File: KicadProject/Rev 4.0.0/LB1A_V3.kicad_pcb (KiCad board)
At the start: 6 copper layers, 42 x 42 mm, 187 parts, among them J601 2337019-1, J602 2337019-1, U101 STM32MP157CAA3, U201 AS4C256M16D3LC-12BCN, U401 STPMIC1xPQR, U501 S40FC004C1B2C00000, U601 LBEE59B1LV-278, U701 DF40C-70DP-0.4V(51), U702 DF40C-100DP-0.4V(51), U703 DF40C-100DP-0.4V(51), X101 32.768kHz, Y101 24MHz

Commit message: power planes
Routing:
- net PMIC_LDO5_2V9: track 0.75 -> 10.7 mm, vias 1 -> 3
- net PMIC_VOUT4_3V3: vias 3 -> 7
- added copper zone on B.Cu, net PMIC_VOUT4_3V3
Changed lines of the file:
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@@
     (thickness 1.2)
     (drawings 8)
-    (tracks 720)
+    (tracks 734)
     (zones 0)
     (modules 187)
@@
   )
   (setup
-    (last_trace_width 0.254)
+    (last_trace_width 0.4)
     (user_trace_width 0.1)
     (user_trace_width 0.127)
@@
   (segment (start 180.5 103.5) (end 180 103.5) (width 0.2) (layer L1_Sig_Pwr.Cu) (net 13))
   (via (at 180.5 103.5) (size 0.4) (drill 0.2) (layers L1_Sig_Pwr.Cu L6_Sig_Pwr.Cu) (net 13))
+  (via (at 172.4 104.1) (size 0.4) (drill 0.2) (layers L1_Sig_Pwr.Cu L6_Sig_Pwr.Cu) (net 13))
+  (via (at 173.6 104.1) (size 0.4) (drill 0.2) (layers L1_Sig_Pwr.Cu L6_Sig_Pwr.Cu) (net 13))
+  (via (at 172.4 104.7) (size 0.4) (drill 0.2) (layers L1_Sig_Pwr.Cu L6_Sig_Pwr.Cu) (net 13))
+  (via (at 173.6 104.7) (size 0.4) (drill 0.2) (layers L1_Sig_Pwr.Cu L6_Sig_Pwr.Cu) (net 13))
   (via (at 179.4 99.6) (size 0.4) (drill 0.2) (layers L1_Sig_Pwr.Cu L6_Sig_Pwr.Cu) (net 18))
   (via (at 172.5 95.6) (size 0.4) (drill 0.2) (layers L1_Sig_Pwr.Cu L6_Sig_Pwr.Cu) (net 18))
@@
   (segment (start 178.746829 98.2) (end 178.675937 98.270892) (width 0.254) (layer L1_Sig_Pwr.Cu) (net 24))
   (segment (start 179.4 98.2) (end 178.746829 98.2) (width 0.254) (layer L1_Sig_Pwr.Cu) (net 24))
+  (segment (start 180.595892 98.270892) (end 180.725 98.4) (width 0.4) (layer L6_Sig_Pwr.Cu) (net 24))
+  (segment (start 178.675937 98.270892) (end 180.595892 98.270892) (width 0.4) (layer L6_Sig_Pwr.Cu) (net 24))
+  (segment (start 180.725 98.4) (end 181.057522 98.4) (width 0.4) (layer L6_Sig_Pwr.Cu) (net 24))
+  (segment (start 181.057522 98.4) (end 181.52499 98.867468) (width 0.4) (layer L6_Sig_Pwr.Cu) (net 24))
+  (segment (start 181.599999 98.942477) (end 181.599999 104.399999) (width 0.4) (layer L6_Sig_Pwr.Cu) (net 24))
+  (segment (start 181.52499 98.867468) (end 181.599999 98.942477) (width 0.4) (layer L6_Sig_Pwr.Cu) (net 24))
+  (via (at 182.1 104.9) (size 0.4) (drill 0.2) (layers L1_Sig_Pwr.Cu L6_Sig_Pwr.Cu) (net 24))
+  (segment (start 181.599999 104.399999) (end 182.1 104.9) (width 0.4) (layer L6_Sig_Pwr.Cu) (net 24))
+  (via (at 182.7 104.9) (size 0.4) (drill 0.2) (layers L1_Sig_Pwr.Cu L6_Sig_Pwr.Cu) (net 24))
+  (segment (start 182.1 104.9) (end 182.7 104.9) (width 0.4) (layer L6_Sig_Pwr.Cu) (net 24))
   (segment (start 183.35 94.75) (end 183.35 93.95) (width 0.127) (layer L1_Sig_Pwr.Cu) (net 35))
   (segment (start 183.35 93.95) (end 183.60402 93.69598) (width 0.127) (layer L1_Sig_Pwr.Cu) (net 35))
@@
         (xy 198.9 116.8) (xy 199.7 116.8) (xy 199.7 116) (xy 200.5 116) (xy 200.5 115.2)
         (xy 201.3 115.2) (xy 201.3 114.4) (xy 201.6 114.4) (xy 201.6 112.5) (xy 213 112.5)
-        (xy 213 130) (xy 185.6 130) (xy 185.6 104.4) (xy 182.8 104.4) (xy 182.8 101)
+        (xy 213 130) (xy 186.5 130) (xy 186.5 104.4) (xy 182.8 104.4) (xy 182.8 101)
         (xy 187.4 101) (xy 187.4 98.1) (xy 182.4 98.1) (xy 182.4 93.1) (xy 189.2 93.1)
       )
@@
       )
     )
+  )
+  (zone (net 13) (net_name PMIC_VOUT4_3V3) (layer L6_Sig_Pwr.Cu) (hatch none 0.508)
+    (connect_pads yes (clearance 0.1))
+    (min_thickness 0.1)
+    (fill yes (arc_segments 32) (thermal_gap 0.508) (thermal_bridge_width 0.508))
+    (polygon
+      (pts
+        (xy 174.8 105) (xy 171 105) (xy 171 102.6) (xy 174.8 102.6)
+      )
+    )

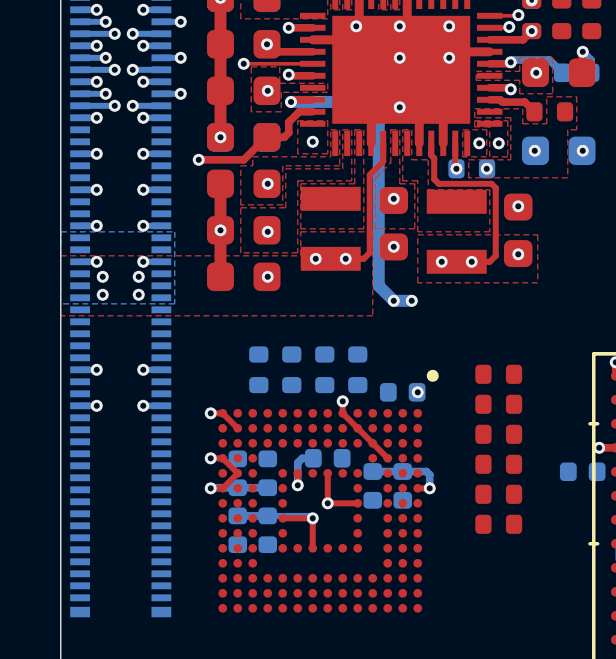
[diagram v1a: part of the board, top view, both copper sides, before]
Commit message: L3 polygon complete
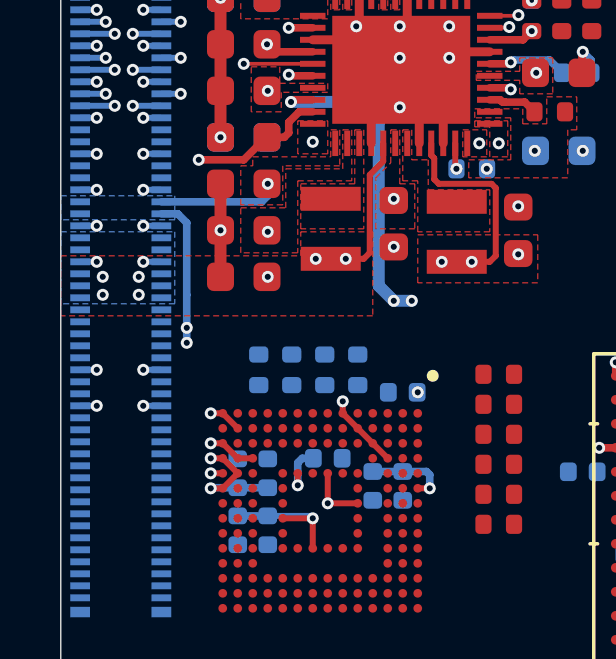
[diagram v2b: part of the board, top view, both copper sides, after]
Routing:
- net PMIC_LDO1_1V8: track 0.00 -> 9.00 mm, vias 1 -> 3
- net PMIC_LDO5_2V9: track 10.7 -> 12.7 mm, vias 3 -> 5
- added copper zone on B.Cu, net PMIC_LDO1_1V8
- added copper zone on L3_Sig_Pwr.Cu, net PMIC_LDO1_1V8
- added copper zone on L3_Sig_Pwr.Cu, net PMIC_LDO5_2V9
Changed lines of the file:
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@@
     (thickness 1.2)
     (drawings 8)
-    (tracks 734)
+    (tracks 751)
     (zones 0)
     (modules 187)
@@
   )
   (setup
-    (last_trace_width 0.4)
+    (last_trace_width 0.254)
     (user_trace_width 0.1)
     (user_trace_width 0.127)
@@
   (segment (start 187.292999 96.872999) (end 186.077001 96.872999) (width 0.254) (layer L6_Sig_Pwr.Cu) (net 20))
   (segment (start 187.72 97.3) (end 187.292999 96.872999) (width 0.254) (layer L6_Sig_Pwr.Cu) (net 20))
+  (segment (start 177.9 101.4) (end 177.9 101) (width 0.254) (layer L6_Sig_Pwr.Cu) (net 21))
+  (segment (start 177.7 101.6) (end 177.9 101.4) (width 0.254) (layer L6_Sig_Pwr.Cu) (net 21))
+  (segment (start 174.355 101.6) (end 177.7 101.6) (width 0.254) (layer L6_Sig_Pwr.Cu) (net 21))
+  (segment (start 174.355 102) (end 174.9 102) (width 0.254) (layer L6_Sig_Pwr.Cu) (net 21))
+  (segment (start 174.9 102) (end 175.2 102.3) (width 0.254) (layer L6_Sig_Pwr.Cu) (net 21))
+  (segment (start 175.2 102.3) (end 175.2 104.7) (width 0.254) (layer L6_Sig_Pwr.Cu) (net 21))
+  (via (at 175.2 105.8) (size 0.4) (drill 0.2) (layers L1_Sig_Pwr.Cu L6_Sig_Pwr.Cu) (net 21))
+  (segment (start 175.2 104.7) (end 175.2 105.8) (width 0.254) (layer L6_Sig_Pwr.Cu) (net 21))
+  (via (at 175.2 106.3) (size 0.4) (drill 0.2) (layers L1_Sig_Pwr.Cu L6_Sig_Pwr.Cu) (net 21))
+  (segment (start 175.2 105.8) (end 175.2 106.3) (width 0.254) (layer L6_Sig_Pwr.Cu) (net 21))
   (segment (start 177.875 99.45) (end 177.85 99.45) (width 0.254) (layer L1_Sig_Pwr.Cu) (net 22))
   (via (at 175.6 100.2) (size 0.4) (drill 0.2) (layers L1_Sig_Pwr.Cu L6_Sig_Pwr.Cu) (net 22))
@@
   (via (at 182.7 104.9) (size 0.4) (drill 0.2) (layers L1_Sig_Pwr.Cu L6_Sig_Pwr.Cu) (net 24))
   (segment (start 182.1 104.9) (end 182.7 104.9) (width 0.4) (layer L6_Sig_Pwr.Cu) (net 24))
+  (segment (start 177.4 110.15) (end 176.9 110.15) (width 0.2) (layer L1_Sig_Pwr.Cu) (net 24))
+  (segment (start 176.9 110.15) (end 176.4 109.65) (width 0.2) (layer L1_Sig_Pwr.Cu) (net 24))
+  (via (at 176 109.649997) (size 0.4) (drill 0.2) (layers L1_Sig_Pwr.Cu L6_Sig_Pwr.Cu) (net 24))
+  (segment (start 176.000003 109.65) (end 176 109.649997) (width 0.2) (layer L1_Sig_Pwr.Cu) (net 24))
+  (segment (start 176.4 109.65) (end 176.000003 109.65) (width 0.2) (layer L1_Sig_Pwr.Cu) (net 24))
+  (via (at 176 110.65) (size 0.4) (drill 0.2) (layers L1_Sig_Pwr.Cu L6_Sig_Pwr.Cu) (net 24))
+  (segment (start 176.4 110.65) (end 176 110.65) (width 0.2) (layer L1_Sig_Pwr.Cu) (net 24))
   (segment (start 183.35 94.75) (end 183.35 93.95) (width 0.127) (layer L1_Sig_Pwr.Cu) (net 35))
   (segment (start 183.35 93.95) (end 183.60402 93.69598) (width 0.127) (layer L1_Sig_Pwr.Cu) (net 35))
@@
       (pts
         (xy 182.3 98.2) (xy 187.3 98.2) (xy 187.3 99) (xy 187.3 100.9) (xy 182.7 100.9)
-        (xy 182.7 102.2) (xy 178.9 102.2) (xy 178.9 103.4) (xy 171 103.4) (xy 171 88)
-        (xy 178.3 88) (xy 178.3 90.3) (xy 182.3 90.3)
+        (xy 182.7 104.4) (xy 178.9 104.4) (xy 171 104.4) (xy 171 88) (xy 178.3 88)
+        (xy 178.3 90.3) (xy 182.3 90.3)
       )
     )
@@
       )
     )
+  )
+  (zone (net 24) (net_name PMIC_LDO5_2V9) (layer L3_Sig_Pwr.Cu) (hatch none 0.508)
+    (connect_pads yes (clearance 0.1))
+    (min_thickness 0.1)
+    (fill yes (arc_segments 32) (thermal_gap 0.508) (thermal_bridge_width 0.508))
+    (polygon
+      (pts
+        (xy 186.4 113.4) (xy 175.7 113.4) (xy 175.7 104.5) (xy 186.4 104.5)
+      )
+    )
+  )
+  (zone (net 21) (net_name PMIC_LDO1_1V8) (layer L6_Sig_Pwr.Cu) (hatch none 0.508)
+    (connect_pads yes (clearance 0.1))
+    (min_thickness 0.1)
+    (fill yes (arc_segments 32) (thermal_gap 0.508) (thermal_bridge_width 0.508))
+    (polygon
+      (pts
+        (xy 174.8 102.2) (xy 171 102.2) (xy 171 101.4) (xy 174.8 101.4)
+      )
+    )
+  )
+  (zone (net 21) (net_name PMIC_LDO1_1V8) (layer L3_Sig_Pwr.Cu) (hatch none 0.508)
+    (connect_pads yes (clearance 0.1))
+    (min_thickness 0.1)
+    (fill yes (arc_segments 32) (thermal_gap 0.508) (thermal_bridge_width 0.508))
+    (polygon
+      (pts
+        (xy 175.6 113.5) (xy 186.4 113.5) (xy 186.4 130) (xy 171 130) (xy 171 104.5)
+        (xy 175.6 104.5)
+      )
+    )
